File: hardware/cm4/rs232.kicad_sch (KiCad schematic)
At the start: 13 parts, among them J3 D340 PC-Schnittstelle, U3 ADuM5211, U5 MAX3232E

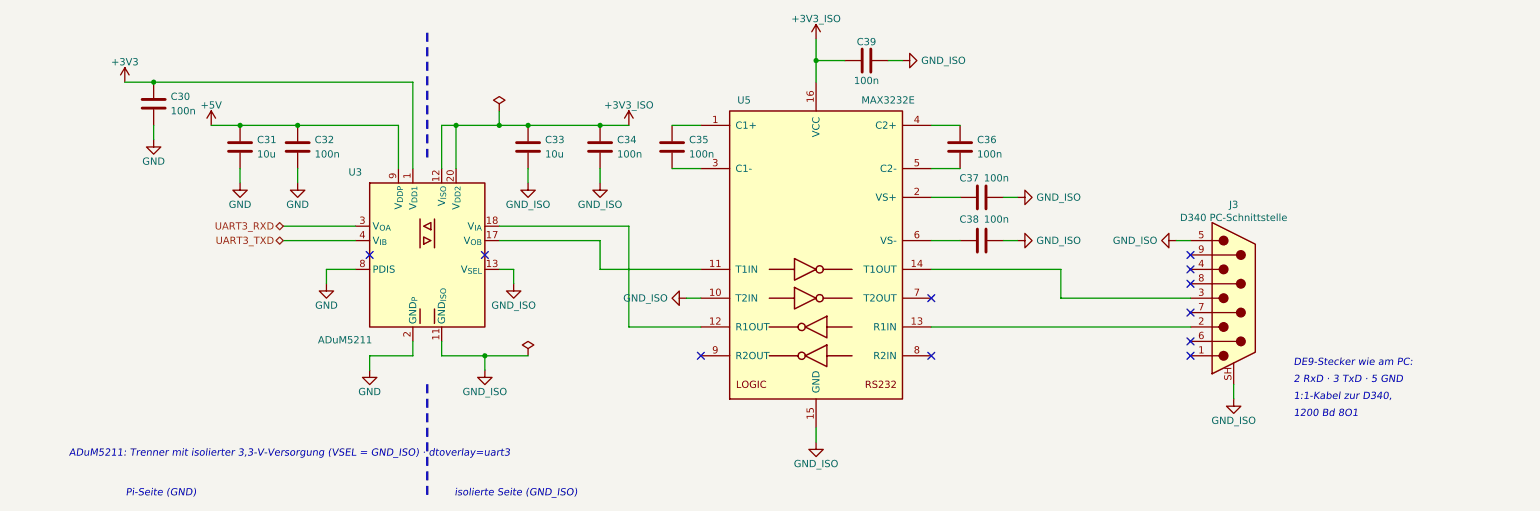
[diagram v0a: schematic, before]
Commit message: CM4-Träger: 4P4C statt DE9, CM4-Platzhalter, ausgerichtete 3D-Modelle
- Serielle Buchse J3: Würth 615004143821 (4P4C), Adapterkabel auf DE9; HAT behält DE9
- M1: CM4 als Platzhalter (Stückliste ja, Bestückungsdaten nein), offizielles STEP 1,5 mm über J11/J12
- 3D-Modelle (Würth RJ45/RJ12/RJ10, Hirose DF40, Bourns SM-LP-5001, ECS-Oszillator) als
  Modellparameter, jede Lage im Rendering geprüft; Herstellermodelle nur lokal (QUELLEN.md)
- richte_3d_aus.py: CM4-Modell laden/verschieben, Lagedatei für die Footprints
- Neu geroutet (0,127 mm Standard), DRC ohne Verstöße, 0 offene Verbindungen

Co-Authored-By: Claude Opus 5.5 <noreply@anthropic.com>
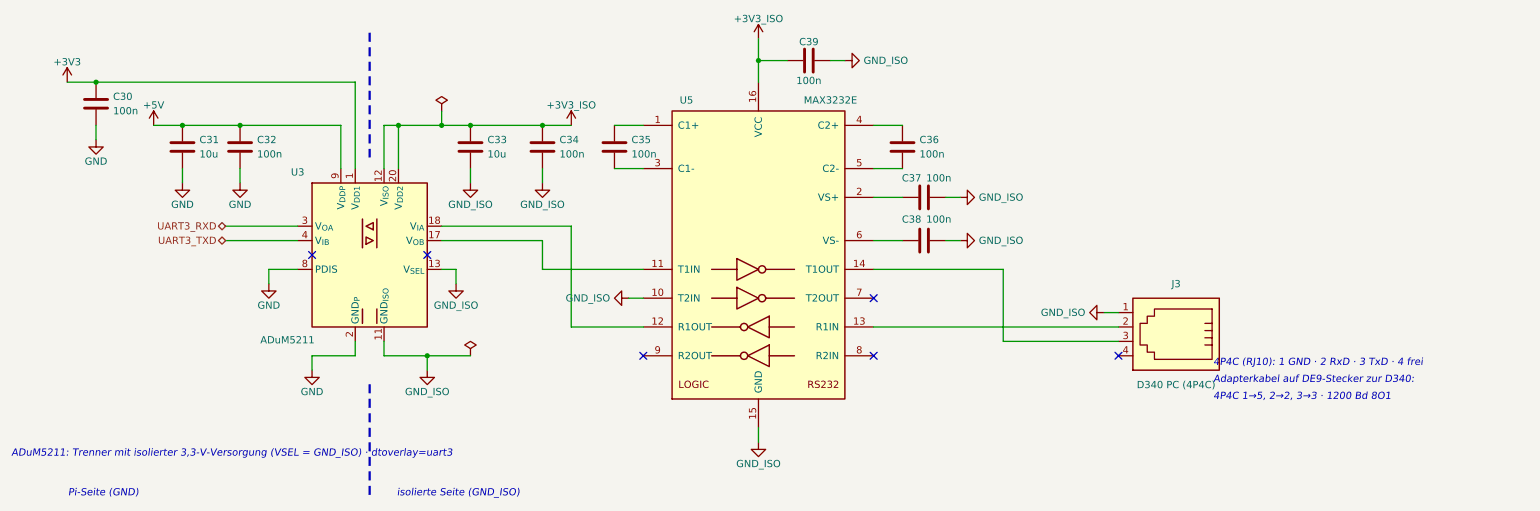
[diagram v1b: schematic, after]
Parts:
- J3: value D340 PC-Schnittstelle -> D340 PC (4P4C); footprint Connector_Dsub:DSUB-9_Pins_Horizontal_P2.77x2.84mm_EdgePinOffset7.70mm_Housed_MountingHolesOffset9.12mm -> Sopho2SIP:RJ10_Wuerth_615004143821_Horizontal; symbol Connector:DE9_Pins_MountingHoles -> Connector:4P4C
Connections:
- net GND_ISO: now also J3.1; no longer J3.5, J3.SH (PAD)
- no-connect marks 11 -> 6
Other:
- note added: "4P4C (RJ10): 1 GND · 2 RxD · 3 TxD · 4 frei"
- note added: "4P4C 1→5, 2→2, 3→3 · 1200 Bd 8O1"
- note added: "Adapterkabel auf DE9-Stecker zur D340:"
- note removed: "1200 Bd 8O1"
- note removed: "1:1-Kabel zur D340,"
- note removed: "2 RxD · 3 TxD · 5 GND"
- note removed: "DE9-Stecker wie am PC:"
- moved on the sheet: C30, C31, C32, C33, C34, C35, C36, C37, C38, C39, U3, U5
